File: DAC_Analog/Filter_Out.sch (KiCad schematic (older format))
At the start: 60 parts

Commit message: Update DAC_analog
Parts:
- removed J? (x2): CONN_01X03, symbol CONN_01X03
- U? (x2): value TC59 -> TC595002ECB
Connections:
- wire segments 188 -> 182
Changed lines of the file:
@@
 P 6050 5650
 F 0 "U?" H 6200 5454 50  0000 C CNN
-F 1 "TC59" H 6050 5850 50  0000 C CNN
+F 1 "TC595002ECB" H 6050 5850 50  0000 C CNN
 F 2 "" H 6050 5650 50  0001 C CNN
 F 3 "" H 6050 5650 50  0001 C CNN
@@
 -6V_anlg
 Connection ~ 5500 5600
-$Comp
-L CONN_01X03 J?
-U 1 1 599B2C1C
-P 6950 2450
-F 0 "J?" H 6950 2650 50  0000 C CNN
-F 1 "CONN_01X03" V 7050 2450 50  0000 C CNN
-F 2 "" H 6950 2450 50  0001 C CNN
-F 3 "" H 6950 2450 50  0001 C CNN
-	1    6950 2450
-	1    0    0    -1
-$EndComp
-$Comp
-L GNDA #PWR?
-U 1 1 599B2D15
-P 6650 2650
-F 0 "#PWR?" H 6650 2400 50  0001 C CNN
-F 1 "GNDA" H 6650 2500 50  0000 C CNN
-F 2 "" H 6650 2650 50  0001 C CNN
-F 3 "" H 6650 2650 50  0001 C CNN
-	1    6650 2650
-	1    0    0    -1
-$EndComp
 Connection ~ 6350 2450
-Wire Wire Line
-	6750 2350 6650 2350
-Wire Wire Line
-	6650 2350 6650 2650
-Wire Wire Line
-	6750 2550 6650 2550
-Connection ~ 6650 2550
 Connection ~ 2650 1550
 Connection ~ 2650 3100
@@
 P 12500 5700
 F 0 "U?" H 12650 5504 50  0000 C CNN
-F 1 "TC59" H 12500 5900 50  0000 C CNN
+F 1 "TC595002ECB" H 12500 5900 50  0000 C CNN
 F 2 "" H 12500 5700 50  0001 C CNN
 F 3 "" H 12500 5700 50  0001 C CNN
@@
 -6V_anlg
 Connection ~ 11950 5650
-$Comp
-L CONN_01X03 J?
-U 1 1 599B41FE
-P 13400 2500
-F 0 "J?" H 13400 2700 50  0000 C CNN
-F 1 "CONN_01X03" V 13500 2500 50  0000 C CNN
-F 2 "" H 13400 2500 50  0001 C CNN
-F 3 "" H 13400 2500 50  0001 C CNN
-	1    13400 2500
-	1    0    0    -1
-$EndComp
-$Comp
-L GNDA #PWR?
-U 1 1 599B4204
-P 13100 2700
-F 0 "#PWR?" H 13100 2450 50  0001 C CNN
-F 1 "GNDA" H 13100 2550 50  0000 C CNN
-F 2 "" H 13100 2700 50  0001 C CNN
-F 3 "" H 13100 2700 50  0001 C CNN
-	1    13100 2700
-	1    0    0    -1
-$EndComp
 Connection ~ 12800 2500
-Wire Wire Line
-	13200 2400 13100 2400
-Wire Wire Line
-	13100 2400 13100 2700
-Wire Wire Line
-	13200 2600 13100 2600
-Connection ~ 13100 2600
 Connection ~ 9100 1600
 Connection ~ 9100 3150

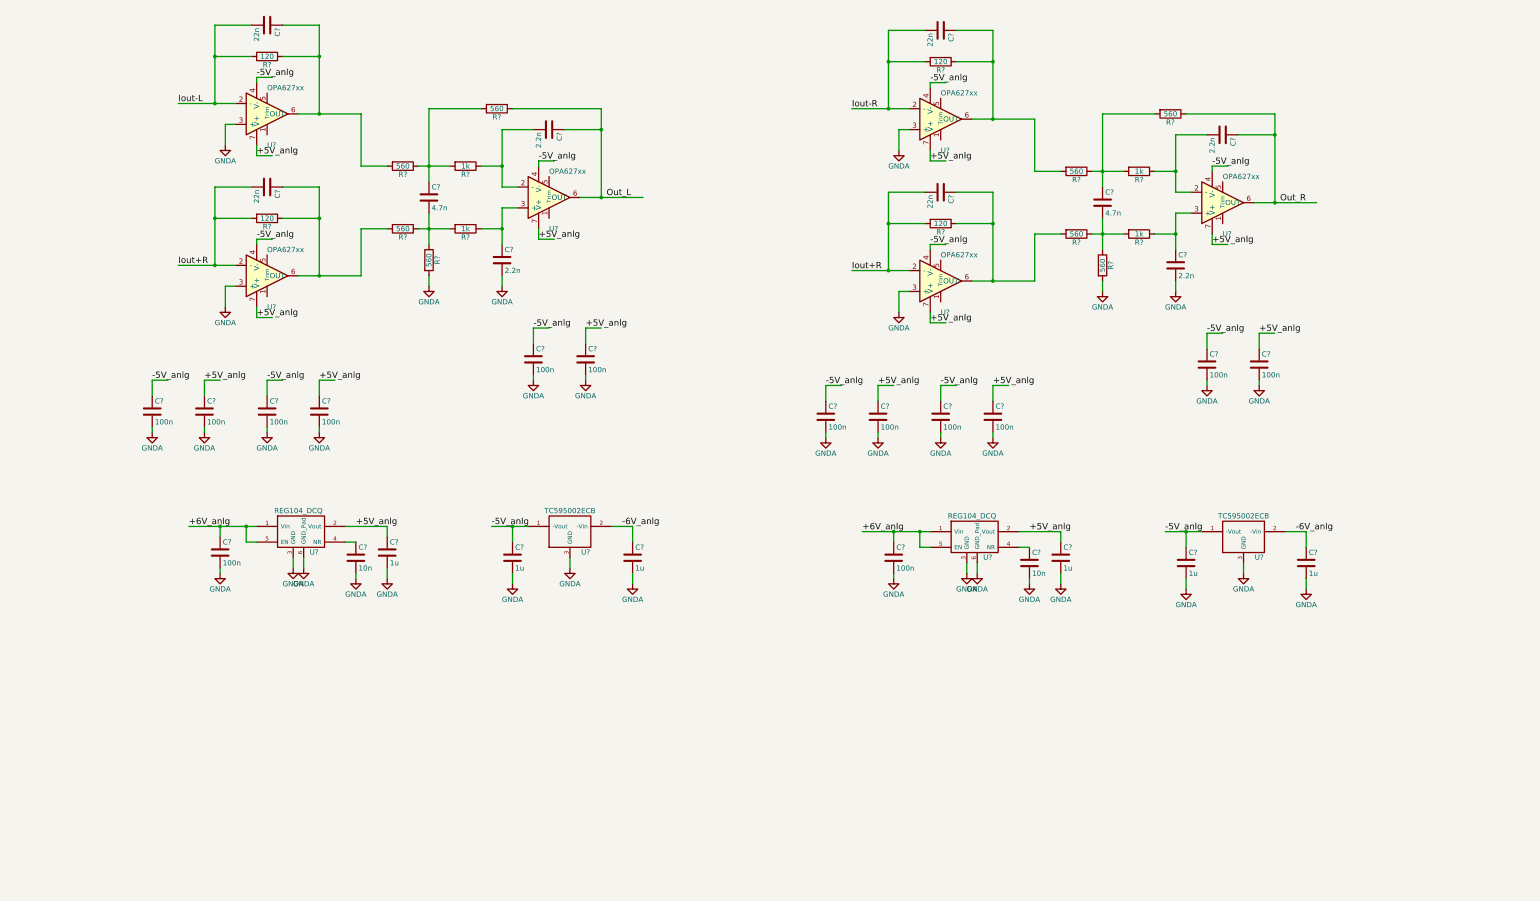
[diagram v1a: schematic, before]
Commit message: Finish DAC_Analog schematic
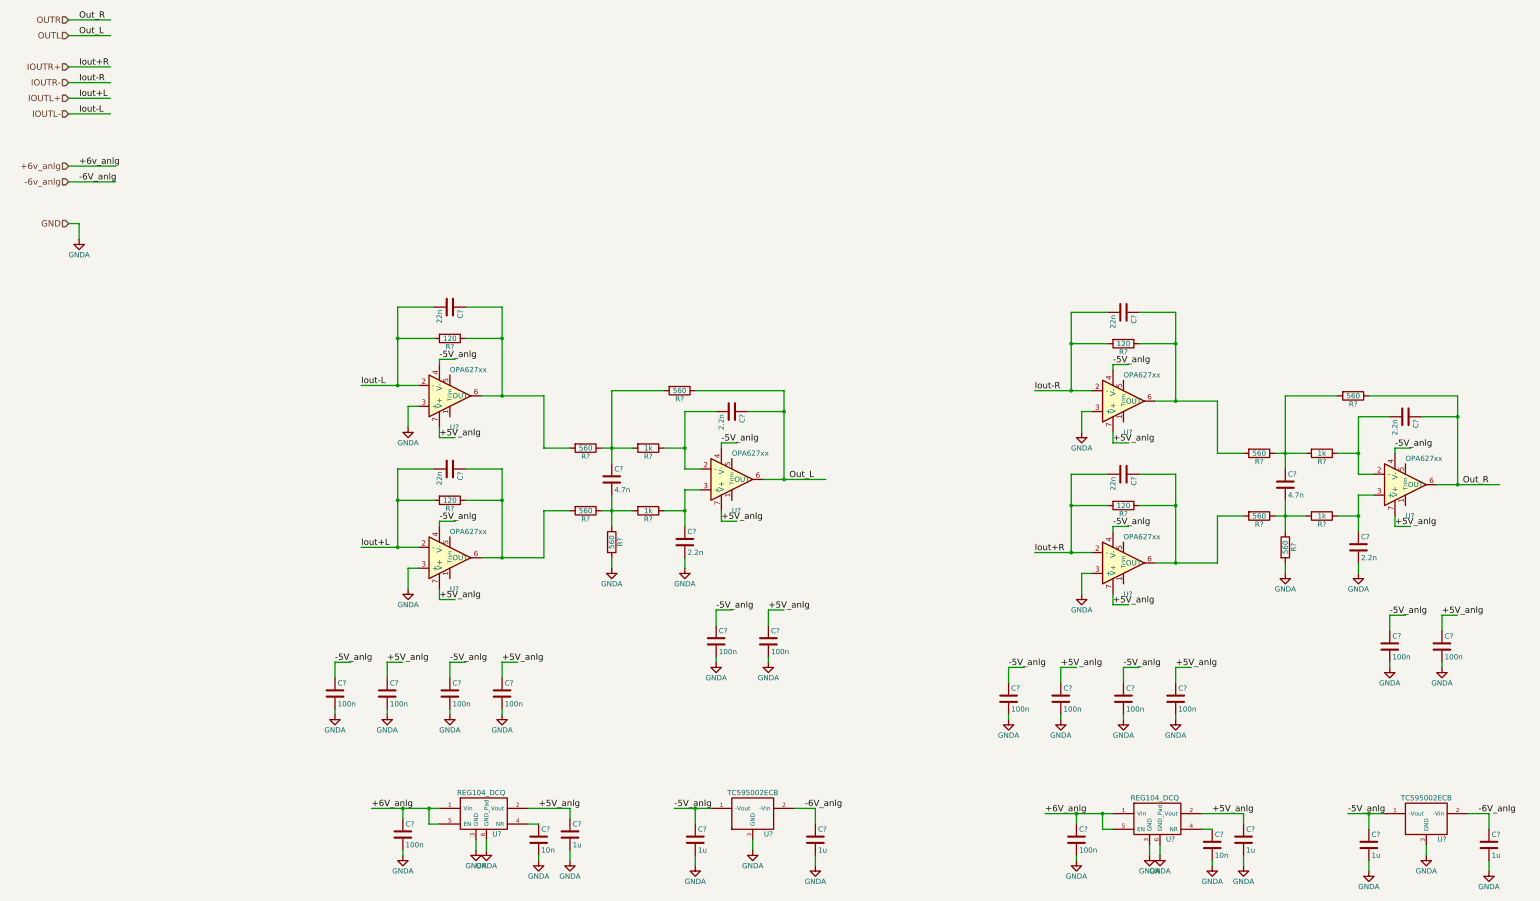
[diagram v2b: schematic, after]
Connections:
- net labels added: +6v_anlg, -6v_anlg, GND, IOUTL+, IOUTL-, IOUTR+, IOUTR-, Iout+L, OUTL, OUTR
- wire segments 182 -> 192
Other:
- moved on the sheet: C?, R?, U?

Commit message: Set footprints
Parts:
- C? (x16): footprint (none) -> Yame_library:SM0603-MR
- C? (x4): footprint (none) -> Yame_library:SM0805-MR
- R? (x16): footprint (none) -> Yame_library:SM1206-MR
- U? (x6): footprint (none) -> Housings_DIP:DIP-8_W7.62mm_Socket_LongPads
- U? (x2): footprint (none) -> TO_SOT_Packages_SMD:SOT-223-6
- U? (x2): footprint (none) -> Yame_library:SOT23-MR

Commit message: set DAC_Analog footprint
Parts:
- C? (x4): footprint (none) -> Capacitors_THT:C_Rect_L10.3mm_W5.0mm_P7.50mm_MKS4
- C? (x6): footprint (none) -> Capacitors_THT:C_Disc_D11.0mm_W5.0mm_P5.00mm
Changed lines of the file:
@@
 F 0 "C?" H 4925 3600 50  0000 L CNN
 F 1 "22n" H 4925 3400 50  0000 L CNN
-F 2 "" H 4938 3350 50  0001 C CNN
+F 2 "Capacitors_THT:C_Rect_L10.3mm_W5.0mm_P7.50mm_MKS4" H 4938 3350 50  0001 C CNN
 F 3 "" H 4900 3500 50  0001 C CNN
 	1    4900 3500
@@
 F 0 "C?" H 4925 5150 50  0000 L CNN
 F 1 "22n" H 4925 4950 50  0000 L CNN
-F 2 "" H 4938 4900 50  0001 C CNN
+F 2 "Capacitors_THT:C_Rect_L10.3mm_W5.0mm_P7.50mm_MKS4" H 4938 4900 50  0001 C CNN
 F 3 "" H 4900 5050 50  0001 C CNN
 	1    4900 5050
@@
 F 0 "C?" H 6475 5250 50  0000 L CNN
 F 1 "4.7n" H 6475 5050 50  0000 L CNN
-F 2 "" H 6488 5000 50  0001 C CNN
+F 2 "Capacitors_THT:C_Disc_D11.0mm_W5.0mm_P5.00mm" H 6488 5000 50  0001 C CNN
 F 3 "" H 6450 5150 50  0001 C CNN
 	1    6450 5150
@@
 F 0 "C?" H 7625 4600 50  0000 L CNN
 F 1 "2.2n" H 7625 4400 50  0000 L CNN
-F 2 "" H 7638 4350 50  0001 C CNN
+F 2 "Capacitors_THT:C_Disc_D11.0mm_W5.0mm_P5.00mm" H 7638 4350 50  0001 C CNN
 F 3 "" H 7600 4500 50  0001 C CNN
 	1    7600 4500
@@
 F 0 "C?" H 7175 5850 50  0000 L CNN
 F 1 "2.2n" H 7175 5650 50  0000 L CNN
-F 2 "" H 7188 5600 50  0001 C CNN
+F 2 "Capacitors_THT:C_Disc_D11.0mm_W5.0mm_P5.00mm" H 7188 5600 50  0001 C CNN
 F 3 "" H 7150 5750 50  0001 C CNN
 	1    7150 5750
@@
 F 0 "C?" H 11375 3650 50  0000 L CNN
 F 1 "22n" H 11375 3450 50  0000 L CNN
-F 2 "" H 11388 3400 50  0001 C CNN
+F 2 "Capacitors_THT:C_Rect_L10.3mm_W5.0mm_P7.50mm_MKS4" H 11388 3400 50  0001 C CNN
 F 3 "" H 11350 3550 50  0001 C CNN
 	1    11350 3550
@@
 F 0 "C?" H 11375 5200 50  0000 L CNN
 F 1 "22n" H 11375 5000 50  0000 L CNN
-F 2 "" H 11388 4950 50  0001 C CNN
+F 2 "Capacitors_THT:C_Rect_L10.3mm_W5.0mm_P7.50mm_MKS4" H 11388 4950 50  0001 C CNN
 F 3 "" H 11350 5100 50  0001 C CNN
 	1    11350 5100
@@
 F 0 "C?" H 12925 5300 50  0000 L CNN
 F 1 "4.7n" H 12925 5100 50  0000 L CNN
-F 2 "" H 12938 5050 50  0001 C CNN
+F 2 "Capacitors_THT:C_Disc_D11.0mm_W5.0mm_P5.00mm" H 12938 5050 50  0001 C CNN
 F 3 "" H 12900 5200 50  0001 C CNN
 	1    12900 5200
@@
 F 0 "C?" H 14075 4650 50  0000 L CNN
 F 1 "2.2n" H 14075 4450 50  0000 L CNN
-F 2 "" H 14088 4400 50  0001 C CNN
+F 2 "Capacitors_THT:C_Disc_D11.0mm_W5.0mm_P5.00mm" H 14088 4400 50  0001 C CNN
 F 3 "" H 14050 4550 50  0001 C CNN
 	1    14050 4550
@@
 F 0 "C?" H 13625 5900 50  0000 L CNN
 F 1 "2.2n" H 13625 5700 50  0000 L CNN
-F 2 "" H 13638 5650 50  0001 C CNN
+F 2 "Capacitors_THT:C_Disc_D11.0mm_W5.0mm_P5.00mm" H 13638 5650 50  0001 C CNN
 F 3 "" H 13600 5800 50  0001 C CNN
 	1    13600 5800

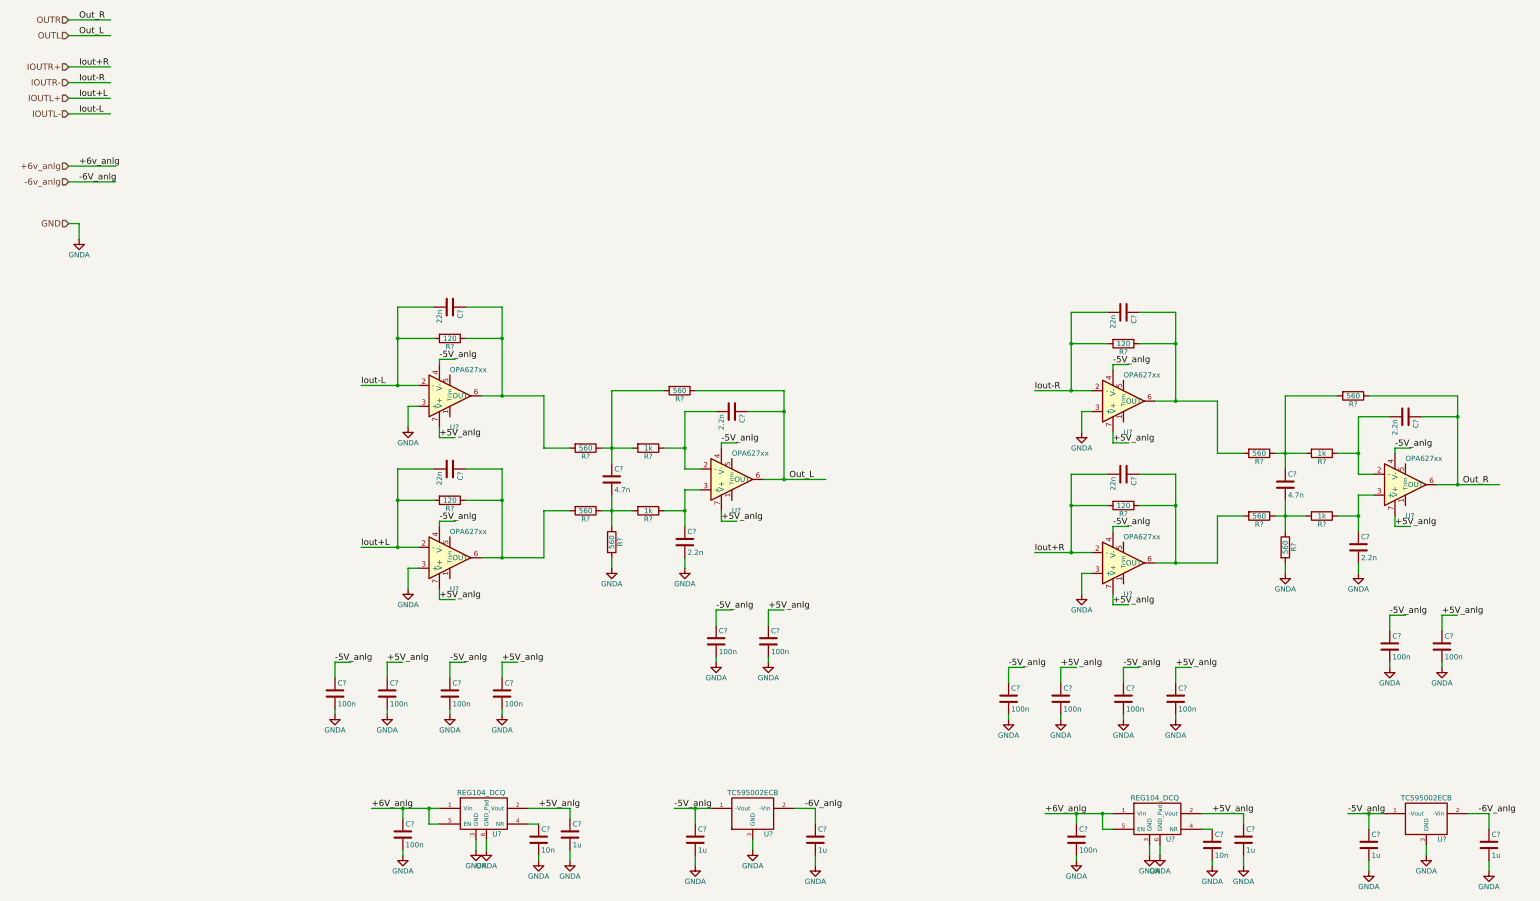
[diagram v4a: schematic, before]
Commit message: Footprint assignment ok
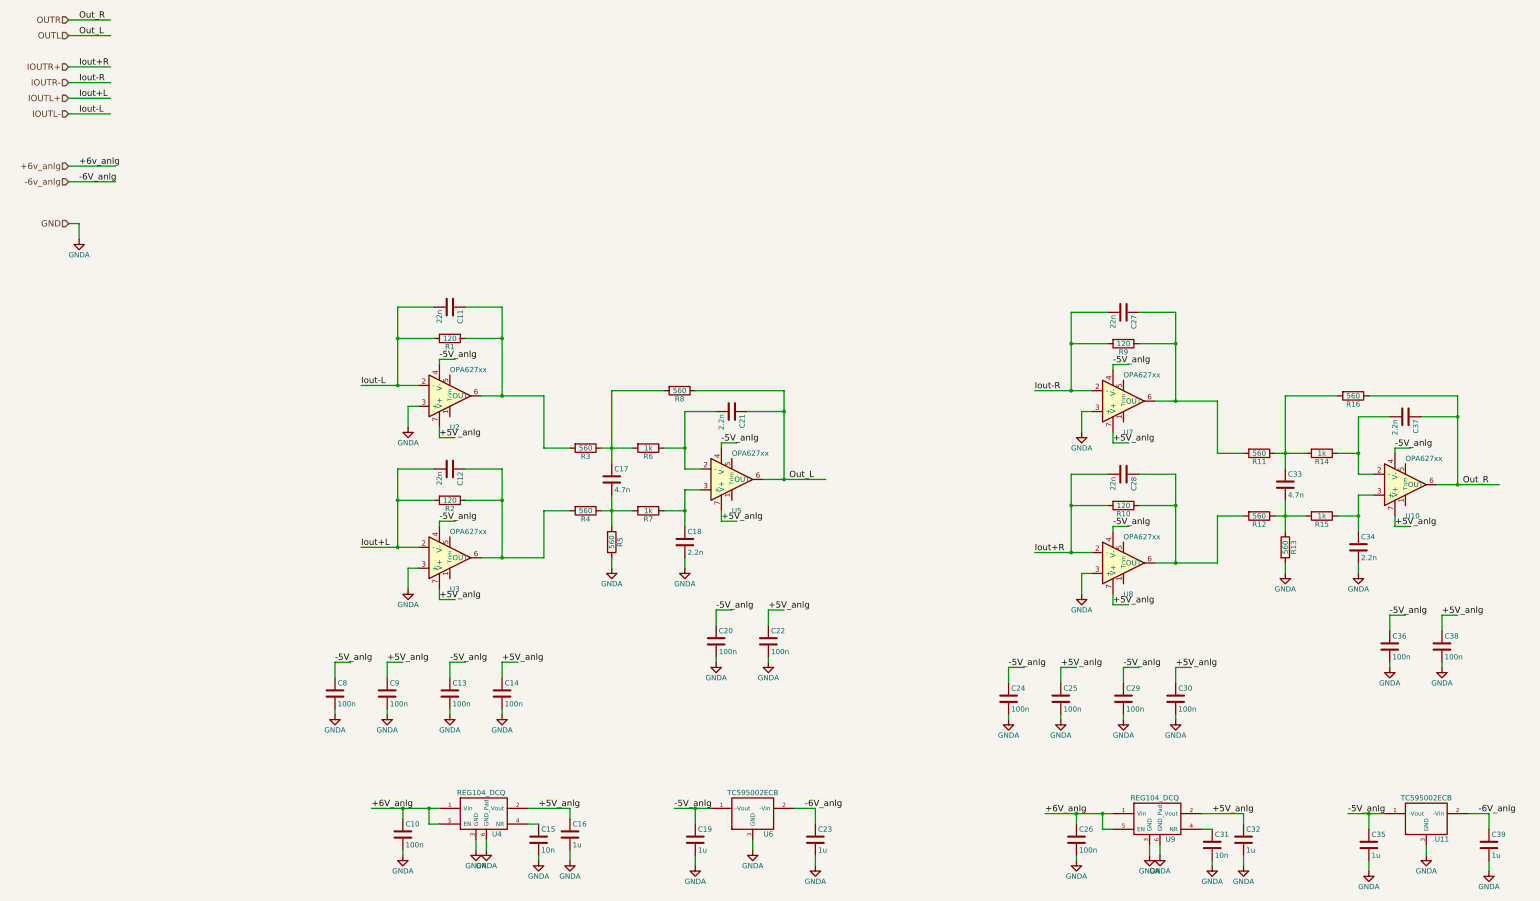
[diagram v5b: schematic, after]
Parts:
- C35, C39: renamed from C?; footprint (none) -> Yame_library:SM0805-MR
- gave numbers to parts that had none: 56

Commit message: Place cmp DAC_Analog
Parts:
- R1, R10, R11, R12, R13, R14, R15, R16, R2, R3, R4, R5, R6, R7, R8, R9: footprint Yame_library:SM1206-MR -> Yame_library:SM0603-MR
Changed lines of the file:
@@
 F 0 "R1" V 4980 3800 50  0000 C CNN
 F 1 "120" V 4900 3800 50  0000 C CNN
-F 2 "Yame_library:SM1206-MR" V 4830 3800 50  0001 C CNN
+F 2 "Yame_library:SM0603-MR" V 4830 3800 50  0001 C CNN
 F 3 "" H 4900 3800 50  0001 C CNN
 	1    4900 3800
@@
 F 0 "R2" V 4980 5350 50  0000 C CNN
 F 1 "120" V 4900 5350 50  0000 C CNN
-F 2 "Yame_library:SM1206-MR" V 4830 5350 50  0001 C CNN
+F 2 "Yame_library:SM0603-MR" V 4830 5350 50  0001 C CNN
 F 3 "" H 4900 5350 50  0001 C CNN
 	1    4900 5350
@@
 F 0 "R3" V 6280 4850 50  0000 C CNN
 F 1 "560" V 6200 4850 50  0000 C CNN
-F 2 "Yame_library:SM1206-MR" V 6130 4850 50  0001 C CNN
+F 2 "Yame_library:SM0603-MR" V 6130 4850 50  0001 C CNN
 F 3 "" H 6200 4850 50  0001 C CNN
 	1    6200 4850
@@
 F 0 "R4" V 6280 5450 50  0000 C CNN
 F 1 "560" V 6200 5450 50  0000 C CNN
-F 2 "Yame_library:SM1206-MR" V 6130 5450 50  0001 C CNN
+F 2 "Yame_library:SM0603-MR" V 6130 5450 50  0001 C CNN
 F 3 "" H 6200 5450 50  0001 C CNN
 	1    6200 5450
@@
 F 0 "R6" V 6880 4850 50  0000 C CNN
 F 1 "1k" V 6800 4850 50  0000 C CNN
-F 2 "Yame_library:SM1206-MR" V 6730 4850 50  0001 C CNN
+F 2 "Yame_library:SM0603-MR" V 6730 4850 50  0001 C CNN
 F 3 "" H 6800 4850 50  0001 C CNN
 	1    6800 4850
@@
 F 0 "R7" V 6880 5450 50  0000 C CNN
 F 1 "1k" V 6800 5450 50  0000 C CNN
-F 2 "Yame_library:SM1206-MR" V 6730 5450 50  0001 C CNN
+F 2 "Yame_library:SM0603-MR" V 6730 5450 50  0001 C CNN
 F 3 "" H 6800 5450 50  0001 C CNN
 	1    6800 5450
@@
 F 0 "R5" V 6530 5750 50  0000 C CNN
 F 1 "560" V 6450 5750 50  0000 C CNN
-F 2 "Yame_library:SM1206-MR" V 6380 5750 50  0001 C CNN
+F 2 "Yame_library:SM0603-MR" V 6380 5750 50  0001 C CNN
 F 3 "" H 6450 5750 50  0001 C CNN
 	1    6450 5750
@@
 F 0 "R8" V 7180 4300 50  0000 C CNN
 F 1 "560" V 7100 4300 50  0000 C CNN
-F 2 "Yame_library:SM1206-MR" V 7030 4300 50  0001 C CNN
+F 2 "Yame_library:SM0603-MR" V 7030 4300 50  0001 C CNN
 F 3 "" H 7100 4300 50  0001 C CNN
 	1    7100 4300
@@
 F 0 "R9" V 11430 3850 50  0000 C CNN
 F 1 "120" V 11350 3850 50  0000 C CNN
-F 2 "Yame_library:SM1206-MR" V 11280 3850 50  0001 C CNN
+F 2 "Yame_library:SM0603-MR" V 11280 3850 50  0001 C CNN
 F 3 "" H 11350 3850 50  0001 C CNN
 	1    11350 3850
@@
 F 0 "R10" V 11430 5400 50  0000 C CNN
 F 1 "120" V 11350 5400 50  0000 C CNN
-F 2 "Yame_library:SM1206-MR" V 11280 5400 50  0001 C CNN
+F 2 "Yame_library:SM0603-MR" V 11280 5400 50  0001 C CNN
 F 3 "" H 11350 5400 50  0001 C CNN
 	1    11350 5400
@@
 F 0 "R11" V 12730 4900 50  0000 C CNN
 F 1 "560" V 12650 4900 50  0000 C CNN
-F 2 "Yame_library:SM1206-MR" V 12580 4900 50  0001 C CNN
+F 2 "Yame_library:SM0603-MR" V 12580 4900 50  0001 C CNN
 F 3 "" H 12650 4900 50  0001 C CNN
 	1    12650 4900
@@
 F 0 "R12" V 12730 5500 50  0000 C CNN
 F 1 "560" V 12650 5500 50  0000 C CNN
-F 2 "Yame_library:SM1206-MR" V 12580 5500 50  0001 C CNN
+F 2 "Yame_library:SM0603-MR" V 12580 5500 50  0001 C CNN
 F 3 "" H 12650 5500 50  0001 C CNN
 	1    12650 5500
@@
 F 0 "R14" V 13330 4900 50  0000 C CNN
 F 1 "1k" V 13250 4900 50  0000 C CNN
-F 2 "Yame_library:SM1206-MR" V 13180 4900 50  0001 C CNN
+F 2 "Yame_library:SM0603-MR" V 13180 4900 50  0001 C CNN
 F 3 "" H 13250 4900 50  0001 C CNN
 	1    13250 4900
@@
 F 0 "R15" V 13330 5500 50  0000 C CNN
 F 1 "1k" V 13250 5500 50  0000 C CNN
-F 2 "Yame_library:SM1206-MR" V 13180 5500 50  0001 C CNN
+F 2 "Yame_library:SM0603-MR" V 13180 5500 50  0001 C CNN
 F 3 "" H 13250 5500 50  0001 C CNN
 	1    13250 5500
@@
 F 0 "R13" V 12980 5800 50  0000 C CNN
 F 1 "560" V 12900 5800 50  0000 C CNN
-F 2 "Yame_library:SM1206-MR" V 12830 5800 50  0001 C CNN
+F 2 "Yame_library:SM0603-MR" V 12830 5800 50  0001 C CNN
 F 3 "" H 12900 5800 50  0001 C CNN
 	1    12900 5800
@@
 F 0 "R16" V 13630 4350 50  0000 C CNN
 F 1 "560" V 13550 4350 50  0000 C CNN
-F 2 "Yame_library:SM1206-MR" V 13480 4350 50  0001 C CNN
+F 2 "Yame_library:SM0603-MR" V 13480 4350 50  0001 C CNN
 F 3 "" H 13550 4350 50  0001 C CNN
 	1    13550 4350
